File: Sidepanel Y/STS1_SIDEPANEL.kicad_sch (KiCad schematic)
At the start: 4 parts, among them J1 Conn_01x08

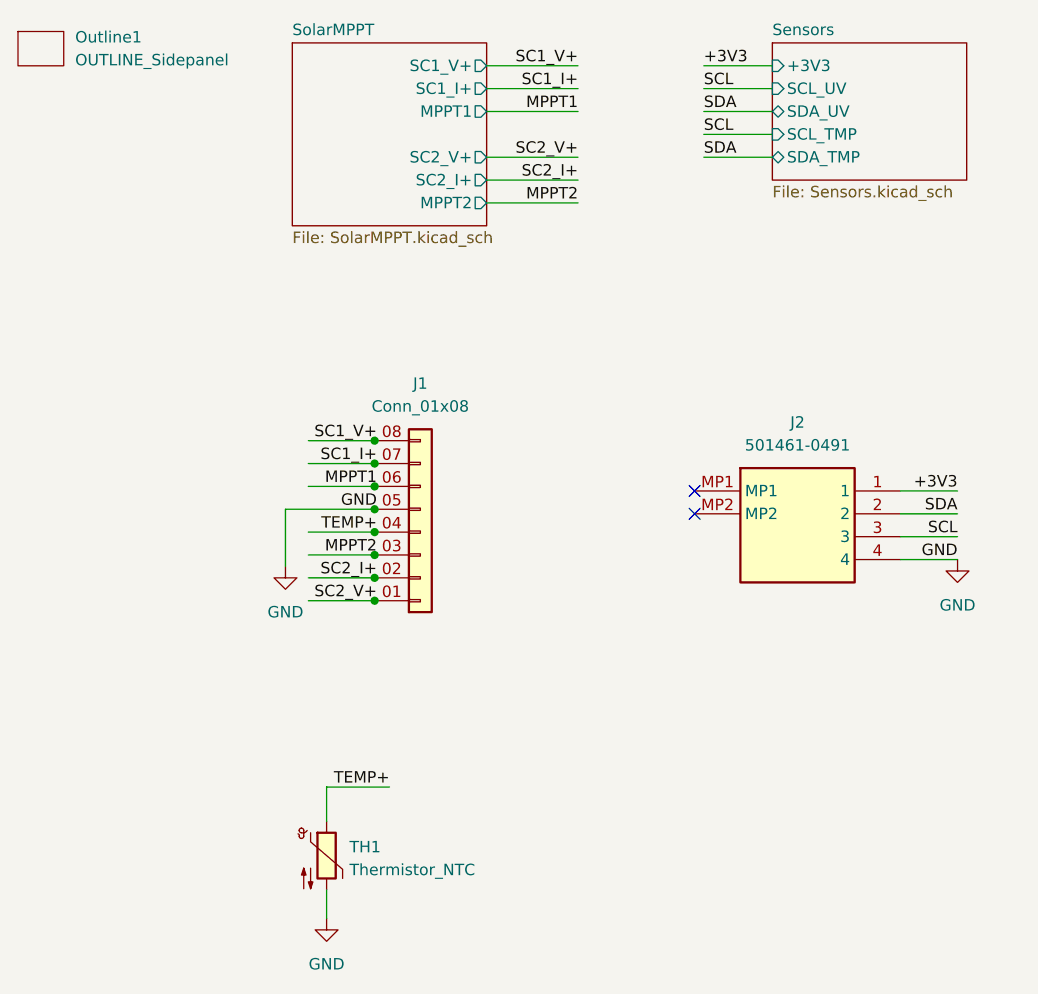
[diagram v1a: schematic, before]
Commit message: Changed the layout of all the sidepanel PCBs to mitigate the problems that arised from the bad previous design.
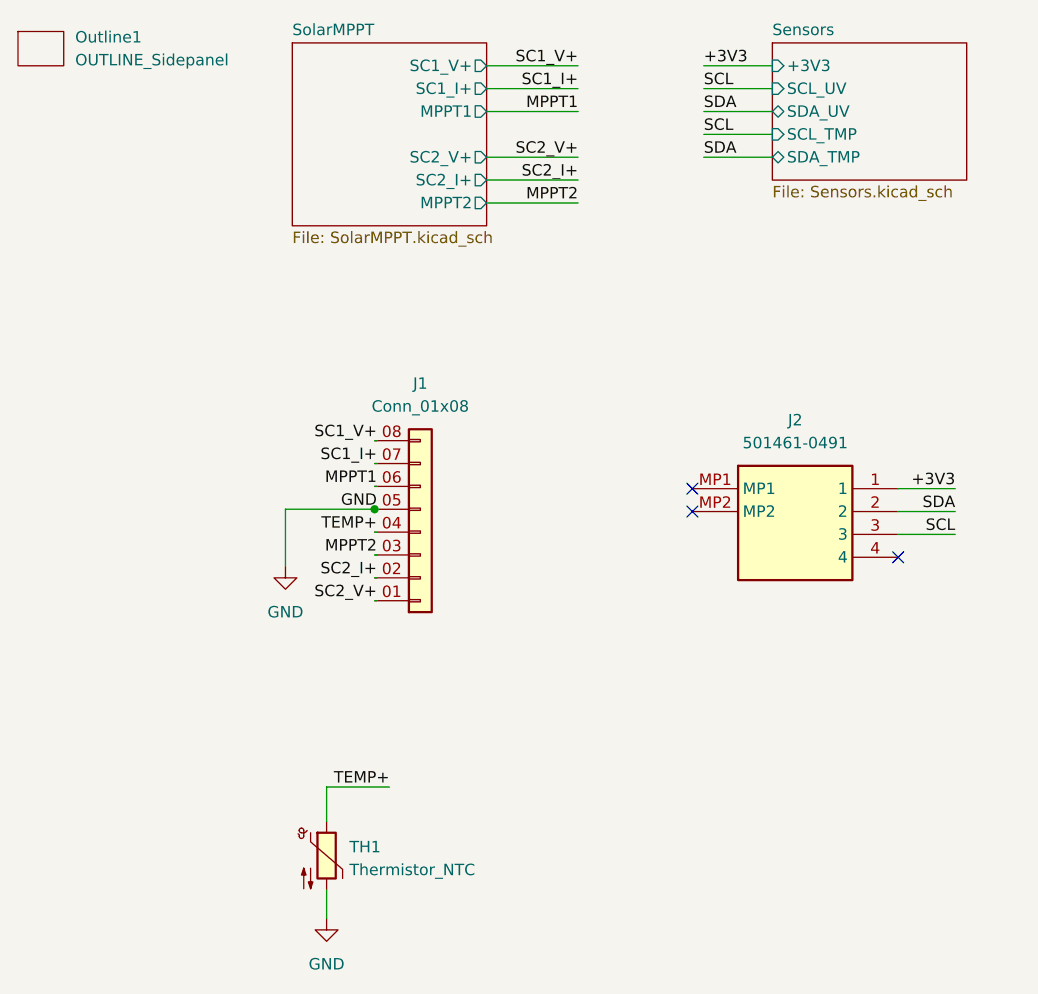
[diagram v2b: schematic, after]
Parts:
- J1: footprint STS_Connector:SAMTEC_ZF5S-08-01-T-WT -> STS_connector:SAMTEC_ZF5S-08-01-T-WT
- Outline1: footprint USER_OUTLINE:OUTLINE_SidepanelY+ -> STS_Sidepanels_Outline:OUTLINE_SidepanelY
- UV1: footprint STS_Connector:5014610491 -> STS_connector:5014610491
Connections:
- net GND: no longer UV1.4
- no-connect marks 2 -> 3

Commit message: Added a  separate ground for the EDU  sensors and did  some small changes for ordering.
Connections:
- net GND1: now reaches UV1.4
- no-connect marks 3 -> 2
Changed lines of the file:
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@@
   (no_connect (at 95.25 78.74))
   (no_connect (at 95.25 76.2))
-  (no_connect (at 118.11 83.82))
   (wire (pts (xy 50.038 78.486) (xy 59.944 78.486))
     (stroke (width 0) (type default))
@@
         )
       )
+    )
+  )
+  (symbol (lib_id "power:GND1") (at 118.11 83.82 90) (unit 1)
+    (in_bom yes) (on_board yes) (dnp no) (fields_autoplaced)
+    (property "Reference" "#PWR01" (at 124.46 83.82 0)
+      (effects (font (size 1.27 1.27)) hide)
+    )
+    (property "Value" "GND1" (at 121.92 83.82 90)
+      (effects (font (size 1.27 1.27)) (justify right))
+    )
+    (property "Footprint" "" (at 118.11 83.82 0)
+      (effects (font (size 1.27 1.27)) hide)
+    )
+    (property "Datasheet" "" (at 118.11 83.82 0)
+      (effects (font (size 1.27 1.27)) hide)
+    )
+    (pin "1")
+    (instances
+      (project "STS1_SIDEPANEL"
+        (path "/e63e39d7-6ac0-4ffd-8aa3-1841a4541b55"
+          (reference "#PWR01") (unit 1)
+        )
+      )

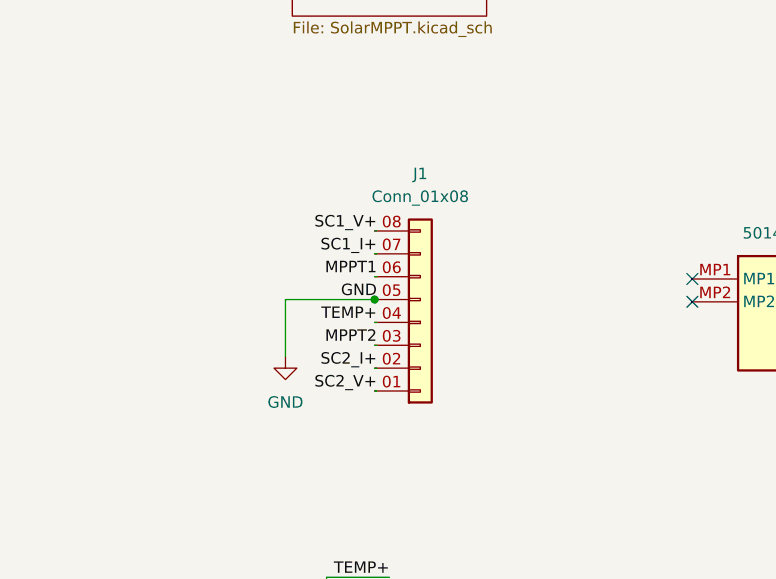
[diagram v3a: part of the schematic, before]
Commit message: moved the connectors, changed the footprint of the input and output capacitors and splitted the input capacitor in two
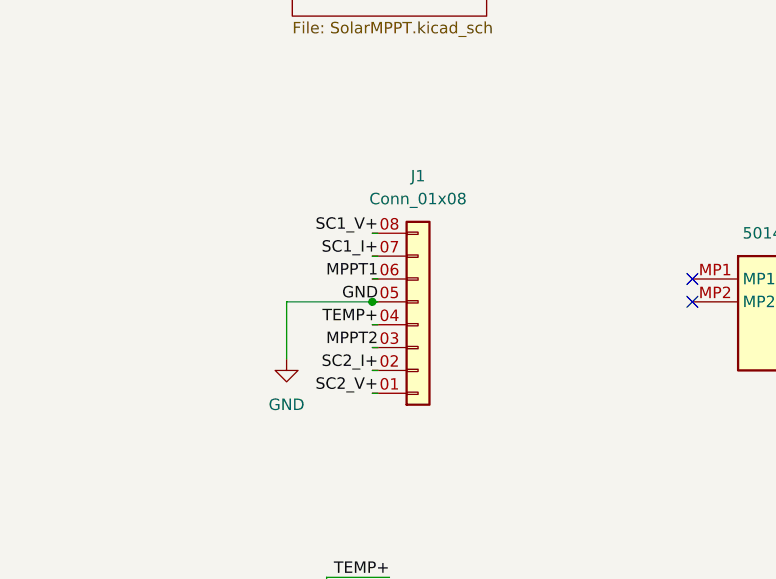
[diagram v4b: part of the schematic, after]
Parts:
- UV1: footprint STS_connector:5014610491 -> STS_connector:200528-0040
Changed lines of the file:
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@@
 (kicad_sch (version 20230121) (generator eeschema)
   (paper "A4")
-  (junction (at 59.944 78.486) (diameter 0) (color 0 0 0 0)
+  (junction (at 59.69 78.74) (diameter 0) (color 0 0 0 0)
   )
   (no_connect (at 95.25 78.74))
   (no_connect (at 95.25 76.2))
-  (wire (pts (xy 50.038 78.486) (xy 59.944 78.486))
+  (wire (pts (xy 50.165 78.74) (xy 59.69 78.74))
     (stroke (width 0) (type default))
   )
@@
     (stroke (width 0) (type default))
   )
-  (wire (pts (xy 59.944 70.866) (xy 60.198 70.866))
+  (wire (pts (xy 59.69 78.74) (xy 60.325 78.74))
+    (stroke (width 0) (type default))
+  )
+  (wire (pts (xy 59.69 71.12) (xy 60.325 71.12))
     (stroke (width 0) (type default))
   )
@@
     (stroke (width 0) (type default))
   )
-  (wire (pts (xy 59.944 88.646) (xy 60.198 88.646))
-    (stroke (width 0) (type default))
-  )
-  (wire (pts (xy 59.944 75.946) (xy 60.198 75.946))
+  (wire (pts (xy 59.69 88.9) (xy 60.325 88.9))
+    (stroke (width 0) (type default))
+  )
+  (wire (pts (xy 59.69 76.2) (xy 60.325 76.2))
     (stroke (width 0) (type default))
   )
@@
     (stroke (width 0) (type default))
   )
-  (wire (pts (xy 50.038 84.836) (xy 50.038 78.486))
-    (stroke (width 0) (type default))
-  )
-  (wire (pts (xy 59.944 78.486) (xy 60.198 78.486))
+  (wire (pts (xy 50.165 85.09) (xy 50.165 78.74))
     (stroke (width 0) (type default))
   )
@@
     (stroke (width 0) (type default))
   )
-  (wire (pts (xy 59.944 73.406) (xy 60.198 73.406))
+  (wire (pts (xy 59.69 73.66) (xy 60.325 73.66))
     (stroke (width 0) (type default))
   )
@@
     (stroke (width 0) (type default))
   )
-  (wire (pts (xy 59.944 86.106) (xy 60.198 86.106))
+  (wire (pts (xy 59.69 86.36) (xy 60.325 86.36))
     (stroke (width 0) (type default))
   )
@@
     (stroke (width 0) (type default))
   )
-  (wire (pts (xy 59.944 83.566) (xy 60.198 83.566))
-    (stroke (width 0) (type default))
-  )
-  (wire (pts (xy 59.944 81.026) (xy 60.198 81.026))
+  (wire (pts (xy 59.69 83.82) (xy 60.325 83.82))
+    (stroke (width 0) (type default))
+  )
+  (wire (pts (xy 59.69 81.28) (xy 60.325 81.28))
     (stroke (width 0) (type default))
   )
@@
     (stroke (width 0) (type default))
   )
-  (label "TEMP+" (at 60.198 81.026 180) (fields_autoplaced)
+  (label "TEMP+" (at 60.325 81.28 180) (fields_autoplaced)
     (effects (font (size 1.27 1.27)) (justify right bottom))
   )
@@
     (effects (font (size 1.27 1.27)) (justify right bottom))
   )
-  (label "MPPT1" (at 60.198 75.946 180) (fields_autoplaced)
+  (label "MPPT1" (at 60.325 76.2 180) (fields_autoplaced)
     (effects (font (size 1.27 1.27)) (justify right bottom))
   )
@@
     (effects (font (size 1.27 1.27)) (justify right bottom))
   )
-  (label "GND" (at 60.198 78.486 180) (fields_autoplaced)
+  (label "GND" (at 60.325 78.74 180) (fields_autoplaced)
     (effects (font (size 1.27 1.27)) (justify right bottom))
   )
@@
     (effects (font (size 1.27 1.27)) (justify right bottom))
   )
-  (label "SC1_I+" (at 60.198 73.406 180) (fields_autoplaced)
-    (effects (font (size 1.27 1.27)) (justify right bottom))
-  )
-  (label "SC2_I+" (at 60.198 86.106 180) (fields_autoplaced)
+  (label "SC1_I+" (at 60.325 73.66 180) (fields_autoplaced)
+    (effects (font (size 1.27 1.27)) (justify right bottom))
+  )
+  (label "SC2_I+" (at 60.325 86.36 180) (fields_autoplaced)
     (effects (font (size 1.27 1.27)) (justify right bottom))
   )
@@
     (effects (font (size 1.27 1.27)) (justify right bottom))
   )
-  (label "SC1_V+" (at 60.198 70.866 180) (fields_autoplaced)
+  (label "SC1_V+" (at 60.325 71.12 180) (fields_autoplaced)
     (effects (font (size 1.27 1.27)) (justify right bottom))
   )
@@
     (effects (font (size 1.27 1.27)) (justify right bottom))
   )
-  (label "SC2_V+" (at 60.198 88.646 180) (fields_autoplaced)
-    (effects (font (size 1.27 1.27)) (justify right bottom))
-  )
-  (label "MPPT2" (at 60.198 83.566 180) (fields_autoplaced)
+  (label "SC2_V+" (at 60.325 88.9 180) (fields_autoplaced)
+    (effects (font (size 1.27 1.27)) (justify right bottom))
+  )
+  (label "MPPT2" (at 60.325 83.82 180) (fields_autoplaced)
     (effects (font (size 1.27 1.27)) (justify right bottom))
   )
@@
       (effects (font (size 1.27 1.27)) hide)
     )
-    (property "Footprint" "STS_connector:5014610491" (at 95.25 76.2 0)
+    (property "Footprint" "STS_connector:200528-0040" (at 95.25 76.2 0)
       (effects (font (size 1.27 1.27)) hide)
     )
@@
     )
   )
-  (symbol (lib_id "Connector_Generic:Conn_01x08") (at 65.024 81.026 0) (mirror x) (unit 1)
-    (in_bom yes) (on_board yes) (dnp no) (fields_autoplaced)
-    (property "Reference" "J1" (at 65.024 64.516 0)
-      (effects (font (size 1.27 1.27)))
-    )
-    (property "Value" "Conn_01x08" (at 65.024 67.056 0)
-      (effects (font (size 1.27 1.27)))
-    )
-    (property "Footprint" "STS_connector:SAMTEC_ZF5S-08-01-T-WT" (at 65.024 81.026 0)
-      (effects (font (size 1.27 1.27)) hide)
-    )
-    (property "Datasheet" "~" (at 65.024 81.026 0)
+  (symbol (lib_id "Connector_Generic:Conn_01x08") (at 64.77 81.28 0) (mirror x) (unit 1)
+    (in_bom yes) (on_board yes) (dnp no)
+    (property "Reference" "J1" (at 64.77 64.77 0)
+      (effects (font (size 1.27 1.27)))
+    )
+    (property "Value" "Conn_01x08" (at 64.77 67.31 0)
+      (effects (font (size 1.27 1.27)))
+    )
+    (property "Footprint" "STS_connector:SAMTEC_ZF5S-08-01-T-WT" (at 64.77 81.28 0)
+      (effects (font (size 1.27 1.27)) hide)
+    )
+    (property "Datasheet" "~" (at 64.77 81.28 0)
       (effects (font (size 1.27 1.27)) hide)
     )
@@
     )
   )
-  (symbol (lib_id "power:GND") (at 50.038 84.836 0) (unit 1)
-    (in_bom yes) (on_board yes) (dnp no) (fields_autoplaced)
-    (property "Reference" "#PWR0112" (at 50.038 91.186 0)
-      (effects (font (size 1.27 1.27)) hide)
-    )
-    (property "Value" "GND" (at 50.038 89.916 0)
-      (effects (font (size 1.27 1.27)))
-    )
-    (property "Footprint" "" (at 50.038 84.836 0)
-      (effects (font (size 1.27 1.27)) hide)
-    )
-    (property "Datasheet" "" (at 50.038 84.836 0)
-      (effects (font (size 1.27 1.27)) hide)
-    )
+  (symbol (lib_id "power:GND") (at 50.165 85.09 0) (unit 1)
+    (in_bom yes) (on_board yes) (dnp no) (fields_autoplaced)
+    (property "Reference" "#PWR0112" (at 50.165 91.44 0)
+      (effects (font (size 1.27 1.27)) hide)
+    )
+    (property "Value" "GND" (at 50.165 90.17 0)
+      (effects (font (size 1.27 1.27)))
+    )
+    (property "Footprint" "" (at 50.165 85.09 0)
+      (effects (font (size 1.27 1.27)) hide)
+    )
+    (property "Datasheet" "" (at 50.165 85.09 0)
+      (effects (font (size 1.27 1.27)) hide)
+    )
